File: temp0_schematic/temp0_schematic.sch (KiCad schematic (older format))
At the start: 16 parts, among them U1 Pro_Trinket_5V, U2 ESP-01, U3 oled_I2C_ssd1306, U4 hdc1080, U5 3.3V_REG

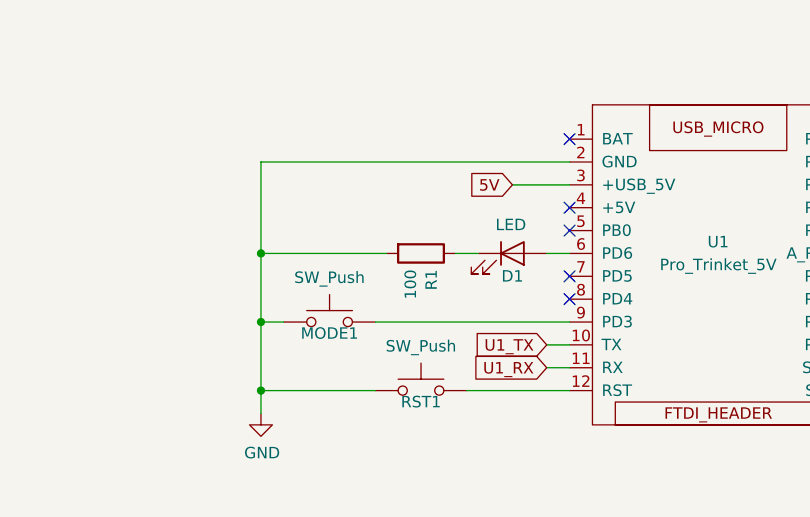
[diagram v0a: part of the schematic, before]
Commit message: Working on the schematic.  Added header for external button.
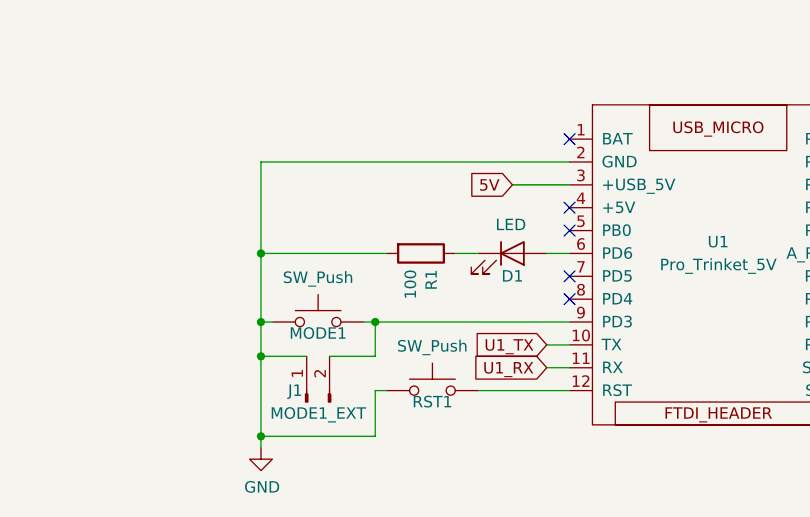
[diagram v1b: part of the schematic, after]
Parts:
- added J1: MODE1_EXT, Connector_PinHeader_1.27mm:PinHeader_1x02_P1.27mm_Horizontal, symbol Connector:Conn_01x02_Male
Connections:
- net GND: now also J1.1 (Pin_1)
- net at MODE1.2, U1.9 (PD3): now also J1.2 (Pin_2)
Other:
- moved on the sheet: MODE1, RST1
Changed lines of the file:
@@
 EESchema Schematic File Version 4
+LIBS:temp0_schematic-cache
 EELAYER 30 0
 EELAYER END
@@
 L Switch:SW_Push RST1
 U 1 1 5E8093DC
-P 4250 4450
-F 0 "RST1" H 4250 4400 50  0000 C CNN
-F 1 "SW_Push" H 4250 4644 50  0000 C CNN
-F 2 "Button_Switch_SMD:SW_Push_1P1T_NO_6x6mm_H9.5mm" H 4250 4650 50  0001 C CNN
-F 3 "~" H 4250 4650 50  0001 C CNN
-	1    4250 4450
+P 4300 4450
+F 0 "RST1" H 4300 4400 50  0000 C CNN
+F 1 "SW_Push" H 4300 4644 50  0000 C CNN
+F 2 "Button_Switch_SMD:SW_Push_1P1T_NO_6x6mm_H9.5mm" H 4300 4650 50  0001 C CNN
+F 3 "~" H 4300 4650 50  0001 C CNN
+	1    4300 4450
 	1    0    0    -1
 $EndComp
@@
 L power:GND #PWR0104
 U 1 1 5E850B36
-P 3550 4550
-F 0 "#PWR0104" H 3550 4300 50  0001 C CNN
-F 1 "GND" H 3555 4377 50  0000 C CNN
-F 2 "" H 3550 4550 50  0001 C CNN
-F 3 "" H 3550 4550 50  0001 C CNN
-	1    3550 4550
+P 3550 4700
+F 0 "#PWR0104" H 3550 4450 50  0001 C CNN
+F 1 "GND" H 3555 4527 50  0000 C CNN
+F 2 "" H 3550 4700 50  0001 C CNN
+F 3 "" H 3550 4700 50  0001 C CNN
+	1    3550 4700
 	1    0    0    -1
 $EndComp
@@
 L Switch:SW_Push MODE1
 U 1 1 5E85CBA8
-P 3850 4150
-F 0 "MODE1" H 3850 4100 50  0000 C CNN
-F 1 "SW_Push" H 3850 4344 50  0000 C CNN
-F 2 "Button_Switch_SMD:SW_Push_1P1T_NO_6x6mm_H9.5mm" H 3850 4350 50  0001 C CNN
-F 3 "~" H 3850 4350 50  0001 C CNN
-	1    3850 4150
-	1    0    0    -1
-$EndComp
-Wire Wire Line
-	4050 4450 3550 4450
-Wire Wire Line
-	3550 4450 3550 4550
-Wire Wire Line
-	3650 4150 3550 4150
-Wire Wire Line
-	3550 4150 3550 4450
-Connection ~ 3550 4450
-Wire Wire Line
-	4900 4450 4450 4450
-Wire Wire Line
-	4900 4150 4050 4150
+P 3800 4150
+F 0 "MODE1" H 3800 4100 50  0000 C CNN
+F 1 "SW_Push" H 3800 4344 50  0000 C CNN
+F 2 "Button_Switch_SMD:SW_Push_1P1T_NO_6x6mm_H9.5mm" H 3800 4350 50  0001 C CNN
+F 3 "~" H 3800 4350 50  0001 C CNN
+	1    3800 4150
+	1    0    0    -1
+$EndComp
 Wire Wire Line
 	4900 4250 4800 4250
@@
 	1    0    0    -1
 $EndComp
-Wire Wire Line
-	4900 3850 4800 3850
-Wire Wire Line
-	4500 3850 4400 3850
-Wire Wire Line
-	4100 3850 3550 3850
-Wire Wire Line
-	3550 3850 3550 4150
-Connection ~ 3550 4150
 $Comp
 L Device:R R1
@@
 Wire Wire Line
 	4900 3450 3550 3450
-Wire Wire Line
-	3550 3450 3550 3850
-Connection ~ 3550 3850
 NoConn ~ 4900 3950
 NoConn ~ 4900 4050
@@
 NoConn ~ 6200 3450
 NoConn ~ 6200 3350
+$Comp
+L Connector:Conn_01x02_Male J1
+U 1 1 5E8088A4
+P 3750 4500
+F 0 "J1" V 3800 4550 50  0000 C CNN
+F 1 "MODE1_EXT" V 3700 4450 50  0000 C CNN
+F 2 "Connector_PinHeader_1.27mm:PinHeader_1x02_P1.27mm_Horizontal" H 3750 4500 50  0001 C CNN
+F 3 "~" H 3750 4500 50  0001 C CNN
+	1    3750 4500
+	0    -1   -1   0
+$EndComp
+Wire Wire Line
+	3850 4300 4050 4300
+Wire Wire Line
+	4050 4300 4050 4150
+Wire Wire Line
+	4050 4150 4000 4150
+Wire Wire Line
+	3600 4150 3550 4150
+Wire Wire Line
+	3550 4150 3550 4300
+Wire Wire Line
+	3550 4300 3750 4300
+Wire Wire Line
+	3550 4150 3550 3850
+Connection ~ 3550 4150
+Wire Wire Line
+	3550 4700 3550 4650
+Connection ~ 3550 4300
+Wire Wire Line
+	4050 4150 4900 4150
+Connection ~ 4050 4150
+Wire Wire Line
+	4900 3850 4800 3850
+Wire Wire Line
+	4500 3850 4400 3850
+Wire Wire Line
+	4100 3850 3550 3850
+Connection ~ 3550 3850
+Wire Wire Line
+	3550 3850 3550 3450
+Wire Wire Line
+	4100 4450 4050 4450
+Wire Wire Line
+	4050 4450 4050 4650
+Wire Wire Line
+	4050 4650 3550 4650
+Connection ~ 3550 4650
+Wire Wire Line
+	3550 4650 3550 4300
+Wire Wire Line
+	4500 4450 4900 4450
 $EndSCHEMATC

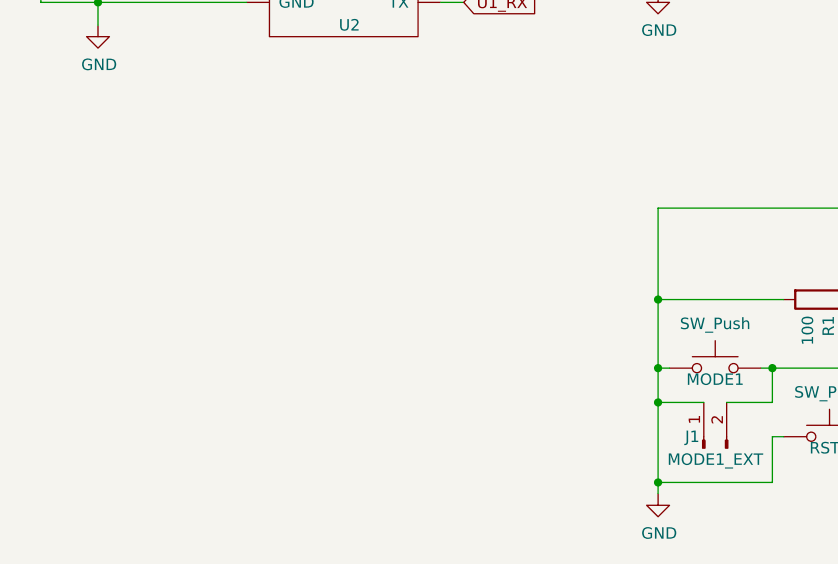
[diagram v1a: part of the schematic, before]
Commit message: Completed first attempt at pcb. Generated gerbers to order fab.
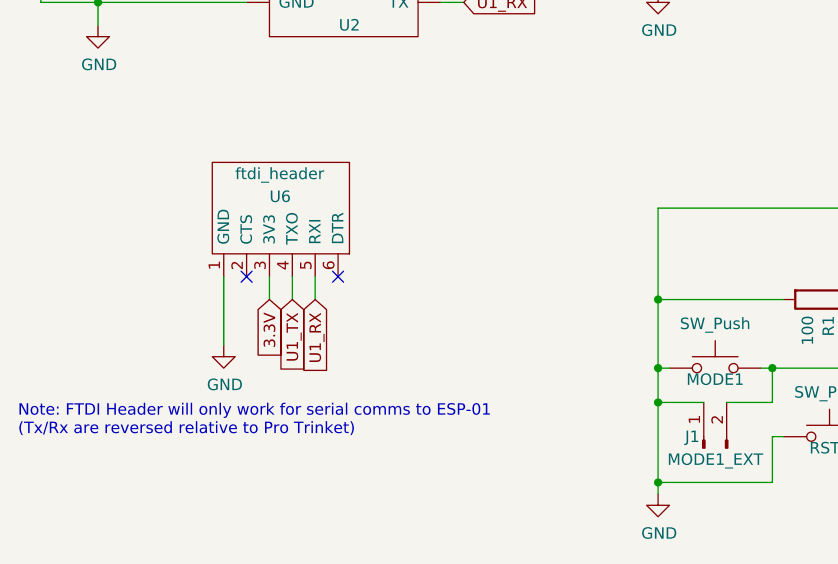
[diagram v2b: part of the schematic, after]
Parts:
- added U6: ftdi_header, Connector_PinHeader_2.54mm:PinHeader_1x06_P2.54mm_Horizontal, symbol temp0_parts:ftdi_header
- J1: footprint Connector_PinHeader_1.27mm:PinHeader_1x02_P1.27mm_Horizontal -> Connector_PinHeader_2.54mm:PinHeader_1x02_P2.54mm_Horizontal
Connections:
- net 3.3V: now also U6.3 (3V3)
- net GND: now also U6.1 (GND)
- net U1_RX: now also U6.5 (RXI)
- net U1_TX: now also U6.4 (TXO)
- no-connect marks 16 -> 18
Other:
- note added: "Note: FTDI Header will only work for serial comms to ESP-01\n(Tx/Rx are reversed relative to Pro Trinket)"
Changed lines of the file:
@@
 F 0 "J1" V 3800 4550 50  0000 C CNN
 F 1 "MODE1_EXT" V 3700 4450 50  0000 C CNN
-F 2 "Connector_PinHeader_1.27mm:PinHeader_1x02_P1.27mm_Horizontal" H 3750 4500 50  0001 C CNN
+F 2 "Connector_PinHeader_2.54mm:PinHeader_1x02_P2.54mm_Horizontal" H 3750 4500 50  0001 C CNN
 F 3 "~" H 3750 4500 50  0001 C CNN
 	1    3750 4500
@@
 Wire Wire Line
 	4500 4450 4900 4450
+Text GLabel 2050 3850 3    50   Input ~ 0
+U1_RX
+Text GLabel 1950 3850 3    50   Input ~ 0
+U1_TX
+Text GLabel 1850 3850 3    50   Input ~ 0
+3.3V
+$Comp
+L power:GND #PWR0107
+U 1 1 5E81FDC4
+P 1650 4050
+F 0 "#PWR0107" H 1650 3800 50  0001 C CNN
+F 1 "GND" H 1655 3877 50  0000 C CNN
+F 2 "" H 1650 4050 50  0001 C CNN
+F 3 "" H 1650 4050 50  0001 C CNN
+	1    1650 4050
+	1    0    0    -1
+$EndComp
+NoConn ~ 2150 3750
+NoConn ~ 1750 3750
+Wire Wire Line
+	1650 4050 1650 3750
+Wire Wire Line
+	1850 3750 1850 3850
+Wire Wire Line
+	1950 3850 1950 3750
+Wire Wire Line
+	2050 3750 2050 3850
+Text Notes 750  4450 0    50   ~ 0
+Note: FTDI Header will only work for serial comms to ESP-01\n(Tx/Rx are reversed relative to Pro Trinket)
+$Comp
+L temp0_parts:ftdi_header U6
+U 1 1 5E82DE8D
+P 1900 3500
+F 0 "U6" H 1850 3600 50  0000 L CNN
+F 1 "ftdi_header" H 1700 3700 50  0000 L CNN
+F 2 "Connector_PinHeader_2.54mm:PinHeader_1x06_P2.54mm_Horizontal" H 1900 3400 50  0001 C CNN
+F 3 "" H 1900 3400 50  0001 C CNN
+	1    1900 3500
+	1    0    0    -1
+$EndComp
 $EndSCHEMATC

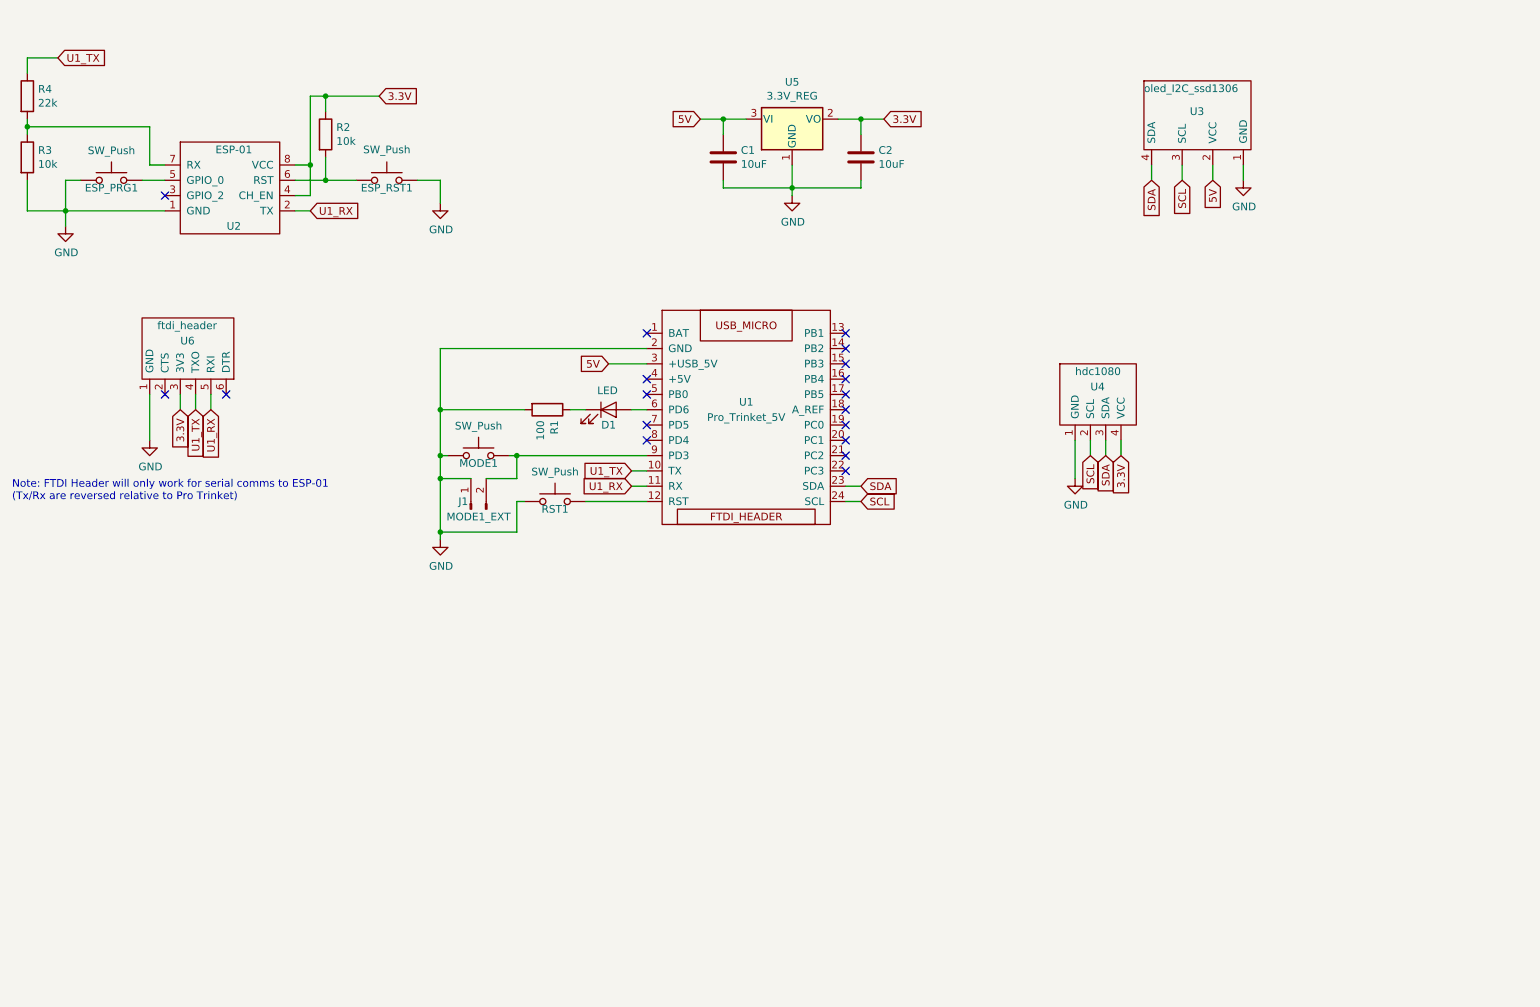
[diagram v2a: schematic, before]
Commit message: Tidied schematic and added pdf to repo.
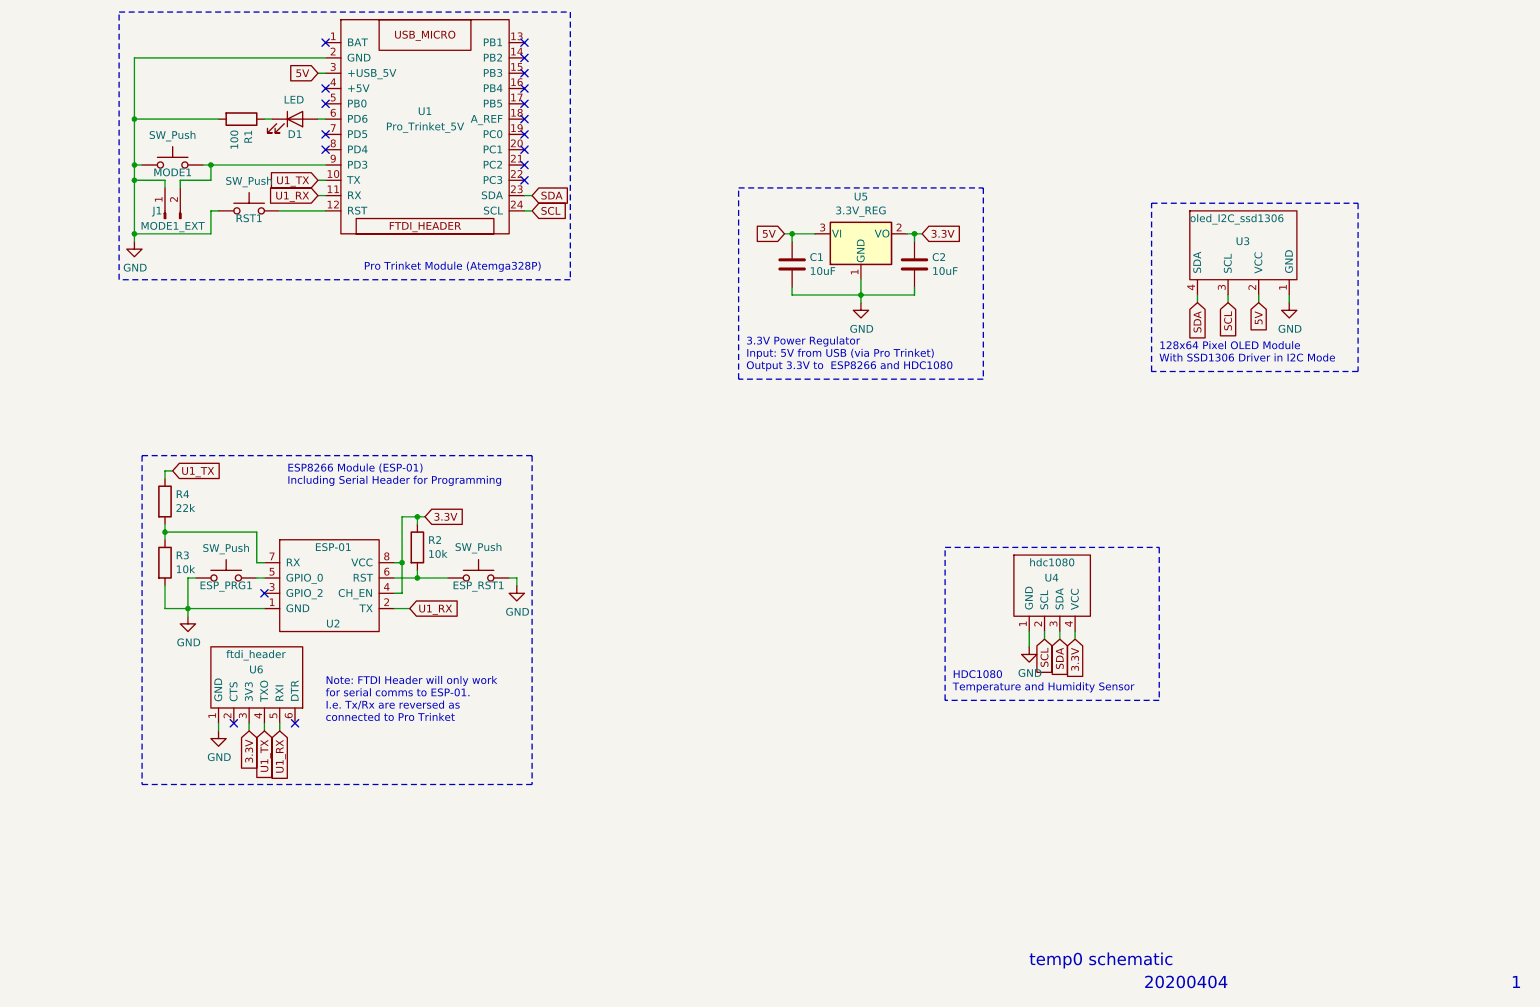
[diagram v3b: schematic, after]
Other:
- note added: "1"
- note added: "128x64 Pixel OLED Module\nWith SSD1306 Driver in I2C Mode"
- note added: "20200404"
- note added: "3.3V Power Regulator\nInput: 5V from USB (via Pro Trinket)\nOutput 3.3V to ESP8266 and HDC1080"
- note added: "ESP8266 Module (ESP-01)\nIncluding Serial Header for Programming"
- note added: "HDC1080\nTemperature and Humidity Sensor"
- note added: "Note: FTDI Header will only work\nfor serial comms to ESP-01.\nI.e. Tx/Rx are reversed as \nconnected to Pro Trinket"
- note added: "Pro Trinket Module (Atemga328P)"
- note added: "temp0 schematic"
- note removed: "Note: FTDI Header will only work for serial comms to ESP-01\n(Tx/Rx are reversed relative to Pro Trinket)"
- moved on the sheet: C1, C2, D1, ESP_PRG1, ESP_RST1, J1, MODE1, R1, R2, R3, R4, RST1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
